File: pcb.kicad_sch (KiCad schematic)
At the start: 9 parts, among them SW1 SW_SPST

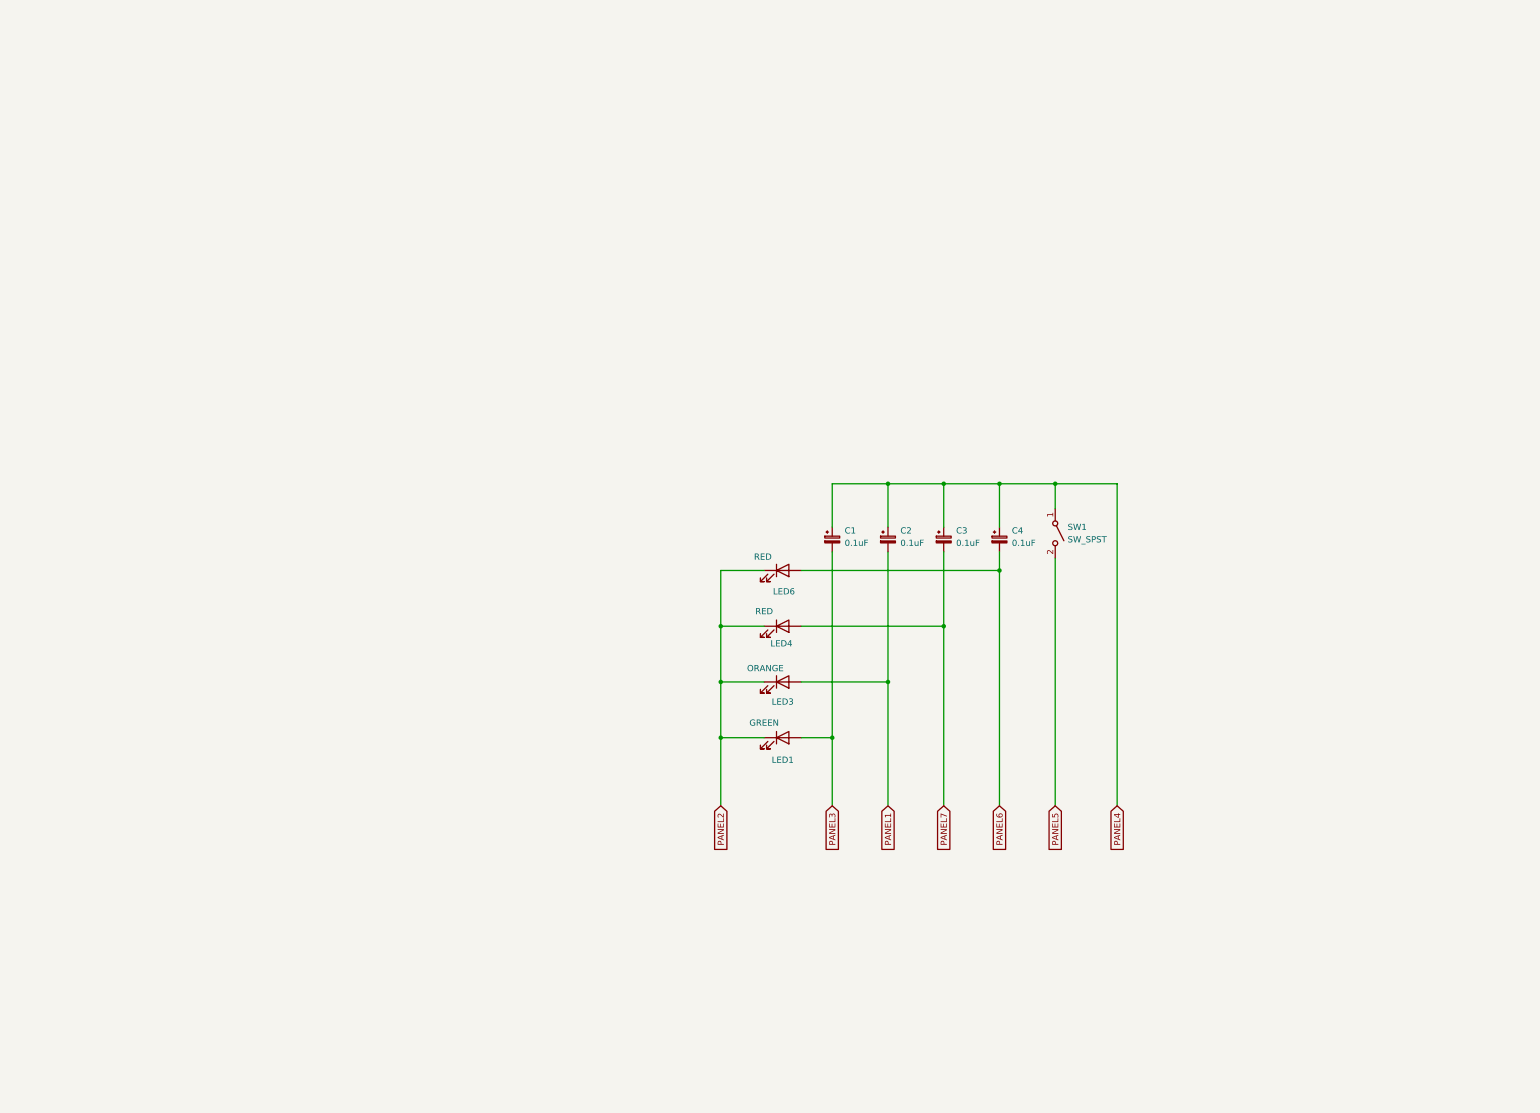
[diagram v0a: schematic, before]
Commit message: Move front panel to its own schematic page
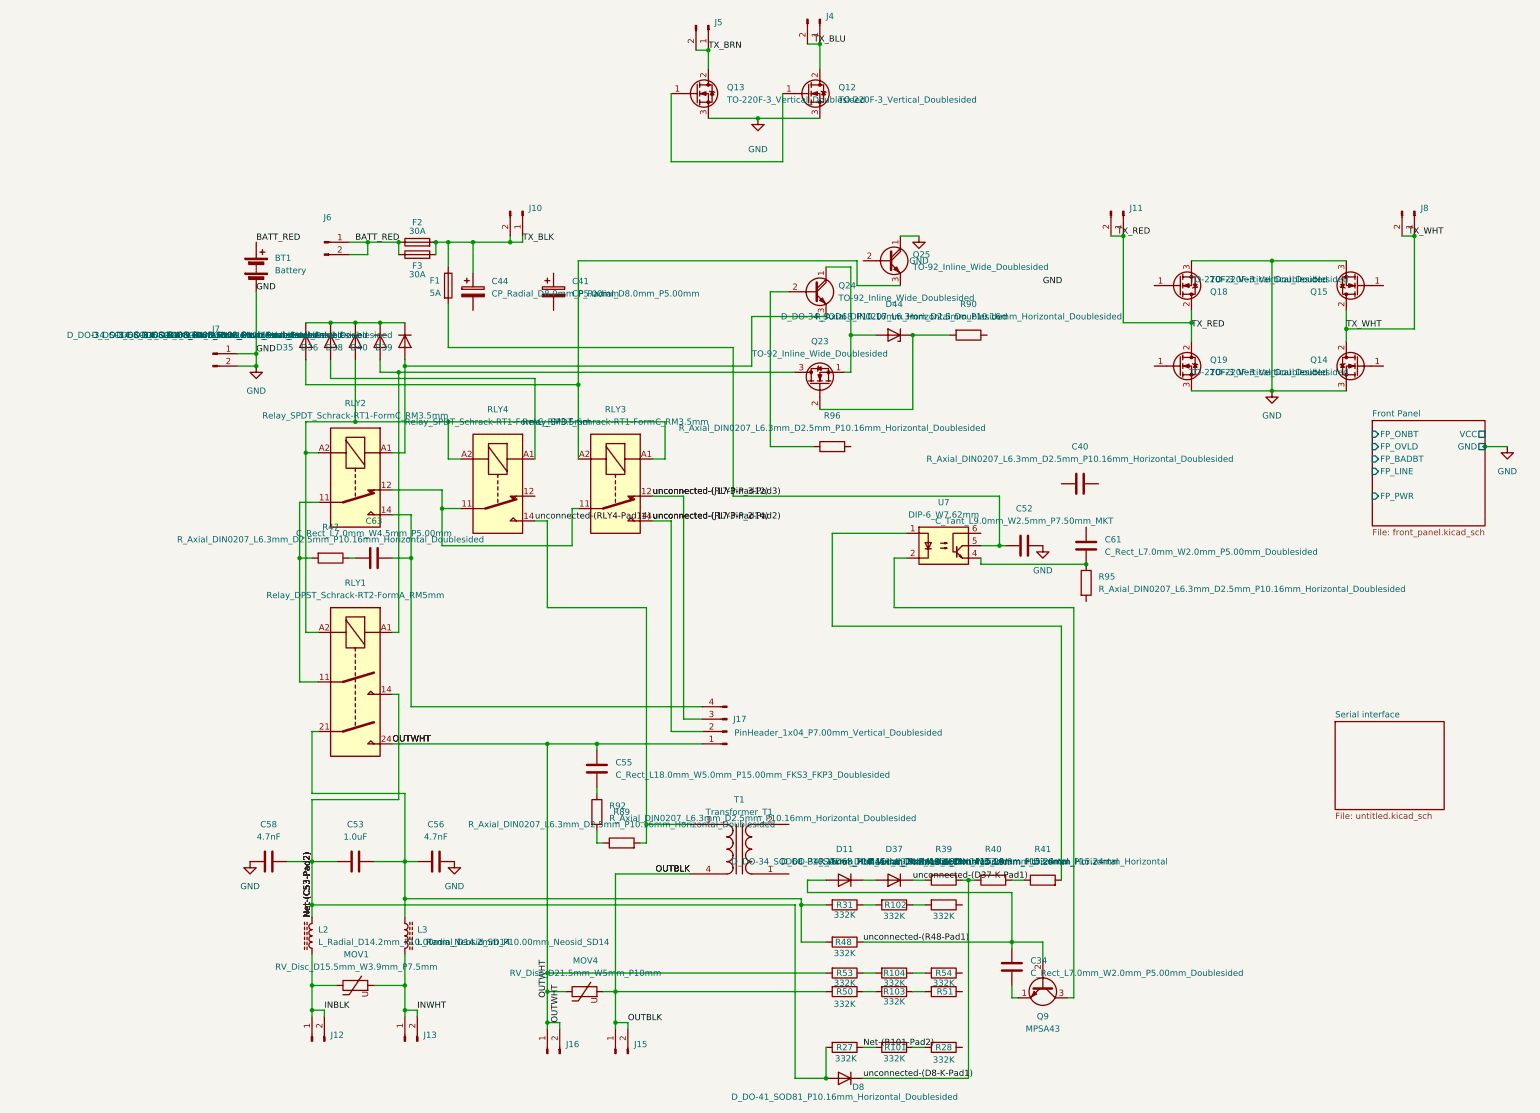
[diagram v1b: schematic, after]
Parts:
- removed C1, C2, C3, C4: 0.1uF, symbol Device:C_Polarized_Small
- removed LED1: GREEN, symbol Device:LED
- removed LED3: ORANGE, symbol Device:LED
- removed LED4, LED6: RED, symbol Device:LED
- removed SW1: SW_SPST, symbol Switch:SW_SPST
- added BT1: Battery, symbol Device:Battery
- added C34, C61: C_Rect_L7.0mm_W2.0mm_P5.00mm_Doublesided, apc-custom:C_Rect_L7.0mm_W2.0mm_P5.00mm_Doublesided, symbol Device:C
- added C40: R_Axial_DIN0207_L6.3mm_D2.5mm_P10.16mm_Horizontal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, apc-custom:C_Rect_L7.2mm_W3.0mm_P5.00mm_FKS2_FKP2_MKS2_MKP2_Doublesided, symbol Device:C
- added C41, C44: CP_Radial_D8.0mm_P5.00mm, Capacitor_THT:CP_Radial_D8.0mm_P5.00mm, symbol Device:C_Polarized
- added C52: C_Tant_L9.0mm_W2.5mm_P7.50mm_MKT, apc-custom:C_Tant_L9.0mm_W2.5mm_P7.50mm_MKT, symbol Device:C
- added C53: 1.0uF, apc-custom:C_Rect_L31.5mm_W13.0mm_P27.50mm_MKS4_Doublesided, symbol Device:C
- added C55: C_Rect_L18.0mm_W5.0mm_P15.00mm_FKS3_FKP3_Doublesi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, apc-custom:C_Rect_L18.0mm_W5.0mm_P15.00mm_FKS3_FKP3_Doublesided, symbol Device:C
- added C56, C58: 4.7nF, Capacitor_THT:C_Disc_D10.0mm_W2.5mm_P5.00mm, symbol Device:C
- added C63: C_Rect_L7.0mm_W4.5mm_P5.00mm, Capacitor_THT:C_Rect_L7.0mm_W4.5mm_P5.00mm, symbol Device:C
- added D11, D35, D36, D37, D38, D39, D40: D_DO-34_SOD68_P10.16mm_Horizontal_Doublesided, apc-custom:D_DO-34_SOD68_P10.16mm_Horizontal_Doublesided, symbol Device:D
- added D44: D_DO-34_SOD68_P10.16mm_Horizontal_Doublesided, apc-custom:D_DO-34_SOD68_P10.16mm_Horizontal_Doublesided, symbol Device:D_Zener
- added D8: D_DO-41_SOD81_P10.16mm_Horizontal_Doublesided, apc-custom:D_DO-41_SOD81_P10.16mm_Horizontal_Doublesided, symbol Device:D
- added F1: 5A, apc-custom:Fuse_PCB_P8.00mm, symbol Device:Fuse
- added F2, F3: 30A, Fuse:Fuse_Blade_ATO_directSolder, symbol Device:Fuse
- added J10, J11, J12, J13, J15, J16, J4, J5, J6, J7, J8: ~, apc-custom:keystone-FASTON, symbol Connector:Conn_01x02_Pin
- added J17: PinHeader_1x04_P7.00mm_Vertical_Doublesided, apc-custom:PinHeader_1x04_P7.00mm_Vertical_Doublesided, symbol Connector:Conn_01x04_Pin
- added L2, L3: L_Radial_D14.2mm_P10.00mm_Neosid_SD14, Inductor_THT:L_Radial_D14.2mm_P10.00mm_Neosid_SD14, symbol Device:L_Ferrite
- added MOV1: RV_Disc_D15.5mm_W3.9mm_P7.5mm, Varistor:RV_Disc_D15.5mm_W3.9mm_P7.5mm, symbol Device:Varistor
- added MOV4: RV_Disc_D21.5mm_W5mm_P10mm, Varistor:RV_Disc_D21.5mm_W5mm_P10mm, symbol Device:Varistor
- added Q12, Q13: TO-220F-3_Vertical_Doublesided, apc-custom:TO-220F-3_Vertical_Doublesided, symbol apc-custom:IRFZ34N
- added Q14, Q15, Q18, Q19: TO-220F-3_Vertical_Doublesided, Package_TO_SOT_THT:TO-220-3_Vertical, symbol apc-custom:PHP54N06T
- added Q23: TO-92_Inline_Wide_Doublesided, apc-custom:TO-92_Inline_Wide_Doublesided, symbol Transistor_FET:2N7000
- added Q24, Q25: TO-92_Inline_Wide_Doublesided, apc-custom:TO-92_Inline_Wide_Doublesided, symbol Transistor_BJT:BC517
- added Q9: MPSA43, Package_TO_SOT_THT:TO-92_Inline, symbol apc-custom:MPSA43
- added R101, R102, R103, R104, R27, R28, R31, R32, R48, R50, R53, R54: 332K, apc-custom:R_Axial_DIN0207_L6.3mm_D2.5mm_P10.16mm_Horizontal_Doublesided, symbol Device:R
- added R39, R40, R41: R_Axial_DIN0411_L9.9mm_D3.6mm_P15.24mm_Horizontal, Resistor_THT:R_Axial_DIN0411_L9.9mm_D3.6mm_P15.24mm_Horizontal, symbol Device:R
- added R47, R51, R89, R90, R92, R95, R96: R_Axial_DIN0207_L6.3mm_D2.5mm_P10.16mm_Horizontal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, apc-custom:R_Axial_DIN0207_L6.3mm_D2.5mm_P10.16mm_Horizontal_Doublesided, symbol Device:R
- added RLY1: Relay_DPST_Schrack-RT2-FormA_RM5mm, Relay_THT:Relay_DPST_Schrack-RT2-FormA_RM5mm, symbol Relay:RT44xxxx
- added RLY2, RLY3, RLY4: Relay_SPDT_Schrack-RT1-FormC_RM3.5mm, Relay_THT:Relay_SPDT_Schrack-RT1-FormC_RM3.5mm, symbol Relay:RT314A12
- added T1: Transformer_T1, apc-custom:Transformer_T1, symbol Device:Transformer_1P_1S
- added U7: DIP-6_W7.62mm, Package_DIP:DIP-6_W7.62mm, symbol Isolator:4N25
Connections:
- new net: C53.1, C56.1, L3.1, R31.2, R48.2, RLY1.21
- new net: R103.1, R51.2
- new net: R103.2, R50.1
- new net: D44.2 (A), Q23.1 (S), Q24.1 (C)
- new net: Q24.2 (B), R96.1
- new net: D39.2 (A), Q24.3 (E), RLY2.A1
- new net: D44.1 (K), Q23.2 (G), R90.2
- new net: R102.2, R31.1
- new net: R40.1, R41.1
- new net: C52.2, F1.2, U7.5
- new net: Q12.1 (G), Q13.1 (G)
- new net: D35.1 (K), D36.1 (K), D38.1 (K), D39.1 (K), D40.1 (K)
- new net: RLY2.12, RLY3.11, RLY4.11
- new net: D38.2 (A), RLY1.A2, RLY2.A2, RLY3.A1, RLY4.A2
- new net: D35.2 (A), Q25.3 (E), RLY3.A2
- new net: D40.2 (A), Q23.3 (D), RLY1.A1
- new net: C34.1, Q9.1 (E)
- new net: C63.1, J17.4 (Pin_4), RLY2.14
- new net: C63.2, R47.1
- new net: Q9.3 (C), U7.2
- new net: R47.2, RLY1.11, RLY2.11
- new net: R104.1, R54.2
- new net: R104.2, R53.1
- new net: D36.2 (A), RLY4.A1
- new net: C61.2, R95.1, U7.4
- new net: R89.1, R92.2
- new net: D11.1 (K), D37.2 (A)
- new net: C55.2, R92.1
- new net: R102.1, R32.2
- new net: R101.1, R28.2
- new net: R41.2, U7.1
- new net BATT_RED: BT1.1 (+), F2.1, F3.1, J6.1 (Pin_1), J6.2 (Pin_2)
- new net GND: BT1.2 (-), C52.1, C56.2, C58.1, J7.1 (Pin_1), J7.2 (Pin_2), Q12.3 (S), Q13.3 (S), Q14.3 (S), Q15.3 (S), Q18.3 (S), Q19.3 (S), Q25.1 (C)
- new net INBLK: J12.1 (Pin_1), J12.2 (Pin_2), L2.1, MOV1.1
- new net INWHT: J13.1 (Pin_1), J13.2 (Pin_2), L3.2, MOV1.2
- new net Net-(C53-Pad2): C53.2, C58.2, D8.2 (A), L2.2, R27.2, RLY1.14
- new net Net-(R101-Pad2): R101.2, R27.1
- new net OUTBLK: J15.1 (Pin_1), J15.2 (Pin_2), MOV4.2, R50.2, T1.4 (SB)
- new net OUTWHT: C55.1, J16.1 (Pin_1), J16.2 (Pin_2), J17.1 (Pin_1), MOV4.1, R53.2, RLY1.24
- new net TX_BLK: C44.1, F1.1, F2.2, F3.2, J10.1 (Pin_1), J10.2 (Pin_2)
- new net TX_BLU: J4.1 (Pin_1), J4.2 (Pin_2), Q12.2 (D)
- new net TX_BRN: J5.1 (Pin_1), J5.2 (Pin_2), Q13.2 (D)
- new net TX_RED: J11.1 (Pin_1), J11.2 (Pin_2), Q18.2 (D), Q19.2 (D)
- new net TX_WHT: J8.1 (Pin_1), J8.2 (Pin_2), Q14.2 (D), Q15.2 (D)
- new net unconnected-(D37-K-Pad1): D37.1 (K), R39.2
- new net unconnected-(D8-K-Pad1): D8.1 (K), R39.1, R40.2
- new net unconnected-(J17-Pin_2-Pad2): J17.2 (Pin_2), RLY3.14
- new net unconnected-(J17-Pin_3-Pad3): J17.3 (Pin_3), RLY3.12
- new net unconnected-(R48-Pad1): C34.2, D11.2 (A), Q9.2 (B), R48.1
- new net unconnected-(RLY4-Pad14): R89.2, RLY4.14, T1.3 (SA)
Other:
- added sheet Front Panel (front_panel.kicad_sch)
- added sheet Serial interface (untitled.kicad_sch)

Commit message: Almost all components added to schematic. Some traces and an IC missing.
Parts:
- removed C53: 1.0uF, apc-custom:C_Rect_L31.5mm_W13.0mm_P27.50mm_MKS4_Doublesided, symbol Device:C
- removed C56, C58: 4.7nF, Capacitor_THT:C_Disc_D10.0mm_W2.5mm_P5.00mm, symbol Device:C
- removed L2, L3: L_Radial_D14.2mm_P10.00mm_Neosid_SD14, Inductor_THT:L_Radial_D14.2mm_P10.00mm_Neosid_SD14, symbol Device:L_Ferrite
- removed MOV1: RV_Disc_D15.5mm_W3.9mm_P7.5mm, Varistor:RV_Disc_D15.5mm_W3.9mm_P7.5mm, symbol Device:Varistor
- removed RLY1: Relay_DPST_Schrack-RT2-FormA_RM5mm, Relay_THT:Relay_DPST_Schrack-RT2-FormA_RM5mm, symbol Relay:RT44xxxx
- added BP1: MagneticBuzzer_ProSignal_ABT-410-RC, Buzzer_Beeper:MagneticBuzzer_ProSignal_ABT-410-RC, symbol Device:Buzzer
- added C10, C11, C12, C21, C22, C23, C57, C60, C62, C67, C9: C_Tant_L9.0mm_W2.5mm_P7.50mm_MKT, apc-custom:C_Tant_L9.0mm_W2.5mm_P7.50mm_MKT, symbol Device:C
- added C13, C14, C32: C_Disc_D4.7mm_W2.5mm_P5.00mm_Doublesided, apc-custom:C_Disc_D4.7mm_W2.5mm_P5.00mm_Doublesided, symbol Device:C
- added C15, C42: C_Radial_D12.5mm_H25.0mm_P5.00mm_Doublesided, apc-custom:C_Radial_D12.5mm_H25.0mm_P5.00mm_Doublesided, symbol Device:C_Polarized
- added C24, C68: C_Tant_L5.0mm_W2.5mm_P5.0mm_MKT_Doublesided, apc-custom:C_Tant_L5.0mm_W2.5mm_P5.0mm_MKT_Doublesided, symbol Device:C
- added C25, C27, C28, C29, C33, C36, C37, C39, C43, C45, C47, C48, C51: C_Rect_L7.0mm_W2.0mm_P5.00mm_Doublesided, apc-custom:C_Rect_L7.0mm_W2.0mm_P5.00mm_Doublesided, symbol Device:C
- added C30, C31, C35, C38, C49, C50: C_Radial_D4.0mm_H7.0mm_P5.00mm_Doublesided, apc-custom:C_Radial_D4.0mm_H7.0mm_P5.00mm_Doublesided, symbol Device:C_Polarized
- added C46: C, symbol Device:C
- added C5, C7, C8: 100nF, apc-custom:C_Tant_L9.0mm_W2.5mm_P7.50mm_MKT, symbol Device:C
- added C6: 100nF, apc-custom:C_Rect_L7.0mm_W2.0mm_P5.00mm_Doublesided, symbol Device:C
- added D10, D12, D13, D14, D15, D16, D25, D26, D27, D28, D29, D30, D31, D32, D33, D42, D45, D46, D7, D9: D_DO-34_SOD68_P10.16mm_Horizontal_Doublesided, apc-custom:D_DO-34_SOD68_P10.16mm_Horizontal_Doublesided, symbol Device:D
- added D17, D18, D19, D20, D21, D22, D23, D24: D_DO-41_SOD81_P10.16mm_Horizontal_Doublesided, apc-custom:D_DO-41_SOD81_P10.16mm_Horizontal_Doublesided, symbol Device:D
- added L1: Inductor_L1, apc-custom:Inductor_L1, symbol Device:L_Ferrite_Coupled
- added L4: L_Axial_L5.0mm_D3.6mm_P10.00mm_Horizontal_Murata_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, Inductor_THT:L_Axial_L5.0mm_D3.6mm_P10.00mm_Horizontal_Murata_BL01RN1A2A2, symbol Device:L
- added L5: L_Axial_L5.3mm_D2.2mm_P10.16mm_Horizontal_Vishay_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, apc-custom:L_Axial_L5.3mm_D2.2mm_P10.16mm_Horizontal_Vishay_IM-1_Doublesided, symbol Device:L
- added Q1: TO-92_Inline_Wide_Doublesided, apc-custom:TO-92_Inline_Wide_Doublesided, symbol apc-custom:MPSA13
- added Q10, Q27, Q3, Q5, Q7: TO-92_Inline_Wide_Doublesided, apc-custom:TO-92_Inline_Wide_Doublesided, symbol apc-custom:KSP2222A
- added Q11, Q2, Q26, Q4, Q6: TO-92_Inline_Wide_Doublesided, apc-custom:TO-92_Inline_Wide_Doublesided, symbol apc-custom:KSP2907A
- added Q28, Q8: TO-92_Inline_Wide_Doublesided, apc-custom:TO-92_Inline_Wide_Doublesided, symbol Transistor_FET:2N7000
- added R1, R100, R105, R106, R107, R108, R12, R13, R16, R17, R18, R19, R2, R20, R21, R22, R23, R24, R26, R29, R3, R30, R33, R34, R36, R37, R38, R4, R42, R43, R44, R45, R46, R49, R5, R52, R55, R56, R57, R58, R59, R6, R60, R61, R62, R63, R64, R66, R67, R68, R69, R7, R70, R71, R72, R73, R74, R75, R76, R77, R78, R79, R8, R82, R83, R86, R87, R88, R9, R91, R97, R98, R99: R_Axial_DIN0207_L6.3mm_D2.5mm_P10.16mm_Horizontal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, apc-custom:R_Axial_DIN0207_L6.3mm_D2.5mm_P10.16mm_Horizontal_Doublesided, symbol Device:R
- added R65: R_Axial_DIN0516_L15.5mm_D5.0mm_P20.32mm_Horizonta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, apc-custom:R_Axial_DIN0516_L15.5mm_D5.0mm_P20.32mm_Horizontal_Doublesided, symbol Device:R
- added U1: DIP-40_W15.24mm_Socket, Package_DIP:DIP-40_W15.24mm_Socket, symbol apc-custom:P87C51FB-4N_SOCKETED
- added U2: DIP-24_W7.62mm, Package_DIP:DIP-24_W7.62mm, symbol apc-custom:ADC0848CCN
- added U3: DIP-8_W7.62mm, Package_DIP:DIP-8_W7.62mm, symbol Memory_EEPROM:93CxxA
- added U5: TO-92_Inline_Wide_Doublesided, apc-custom:TO-92_Inline_Wide_Doublesided, symbol Power_Supervisor:MC34064P
- added U6: DIP-14_W7.62mm_Doublesided, apc-custom:DIP-14_W7.62mm_Doublesided, symbol apc-custom:LM324AN
- added U8: TO-220F-5_P3.4x3.7mm_StaggerEven_Lead3.5mm_Vertic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, Package_TO_SOT_THT:TO-220F-5_P3.4x3.7mm_StaggerEven_Lead3.5mm_Vertical, symbol apc-custom:LM2575T-ADJ
- added U9: DIP-14_W7.62mm_Doublesided, apc-custom:DIP-14_W7.62mm_Doublesided, symbol apc-custom:360-2040B
- added VR1: TO-92_Inline_Wide_Doublesided, apc-custom:TO-92_Inline_Wide_Doublesided, symbol Regulator_Linear:LP2950-5.0_TO92
- added Y1: Crystal_HC52-U_Vertical, Crystal:Crystal_HC52-U_Vertical, symbol Device:Crystal
- C41, C44: value CP_Radial_D8.0mm_P5.00mm -> 330uF 25V
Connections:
- net Front Panel/FP_BADBT: now also R7.1
- net Front Panel/FP_LINE: now also R4.1
- net Front Panel/FP_ONBT: now also R5.1
- net Front Panel/FP_OVLD: now also R6.1
- net Front Panel/FP_PWR: now also R17.1
- net Front Panel/VCC: now also C7.2, R2.2
- net GND: now also C40.1, C41.2, C44.2, C10.2, C11.2, C12.2, C15.2, C21.1, C22.1, C25.1, C28.2, C29.2, C30.2, C31.2, C33.2, C35.2, C37.2, C42.2, C43.2, C45.2, C46.1, C47.1, C48.2, C50.1, C51.1, C57.2, C6.1, C60.1, C62.2, C67.2, C68.1, C7.1, C9.2, D13.2 (A), D19.2 (A), D20.2 (A), D29.1 (K), D32.2 (A), D33.2 (A), D45.2 (A), Q1.1 (C), Q27.1 (E), Q5.1 (E), Q7.1 (E), Q8.1 (S), R100.2, R24.2, R33.1, R44.1, R45.1, R49.1, R57.1, R62.1, R67.1, R69.2, R74.2, R77.2, R8.2, R88.1, U2.10 (AGND), U2.12 (DGND), U3.5 (GND), U5.3 (GND), U6.12 (+), U6.5 (+), U8.3 (GND), U9.5, VR1.2 (GND)
- net TX_BLK: now also D17.1 (K), D18.1 (K)
- net TX_BLU: now also D16.1 (K), D21.2 (A), D22.2 (A)
- net TX_BRN: now also D23.2 (A), D24.2 (A)
- net TX_RED: now also D25.1 (K)
- net TX_WHT: now also D27.1 (K)
- net at C41.1: now also D17.2 (A), D18.2 (A), L1.2, L1.4, R66.1
- net Line in/LIVE_SENSE: now reaches R31.2, R48.2
- net at Q18.1 (G): now also R82.1
- net Line in/RLY_LINE_2: now reaches C52.2, F1.2, U7.5
- net Line in/RLY_LINE_2: now also RLY2.A2, RLY3.A1, RLY4.A2, Q2.1 (C), Q6.1 (C), R36.2
- net at R51.1: now also C36.1, R52.2, U6.9 (-)
- net at Q19.1 (G): now also R83.1
- net Line in/RLY_LINE_1: now reaches D40.2 (A), Q23.3 (D)
- net at Q15.1 (G): now also R79.1
- net Line in/SW_NEUTRAL: now reaches R47.2, RLY2.11
- net at D36.2 (A), RLY4.A1: now also Q27.3 (C)
- net at C61.2, R95.1, U7.4: now also R43.1
- net at R95.2: now also C61.1, U7.6
- net at T1.1 (AA): now also D30.2 (A), D32.1 (K)
- net at T1.2 (AB): now also D31.2 (A), D33.1 (K)
- net at C40.2: now also R60.1, R61.1
- net at R54.1: now also C37.1, R57.2, U6.10 (+)
- net at Q25.2 (B): now also R97.1
- net at Q14.1 (G): now also R78.1
- net at R28.1: now also C27.2, R26.1, U6.2 (-)
- net at R32.1: now also C28.1, R33.2, U6.3 (+)
- net Net-(C53-Pad2) renamed Line in/NEUTRAL_SENSE
- net Net-(R101-Pad2): no longer names the net of R101.2, R27.1
- net unconnected-(D37-K-Pad1): no longer names the net of D37.1 (K), R39.2
- net unconnected-(D8-K-Pad1): no longer names the net of D8.1 (K), R39.1, R40.2
- net unconnected-(J17-Pin_2-Pad2): no longer names the net of J17.2 (Pin_2), RLY3.14
- net unconnected-(J17-Pin_3-Pad3): no longer names the net of J17.3 (Pin_3), RLY3.12
- net unconnected-(R48-Pad1): no longer names the net of C34.2, D11.2 (A), Q9.2 (B), R48.1
- net unconnected-(RLY4-Pad14): no longer names the net of R89.2, RLY4.14, T1.3 (SA)
- new net: C33.1, D12.1 (K), Q8.2 (G), R45.2
- new net: C31.1, R38.1, VR1.3 (VI)
- new net: R29.1, R30.1, U6.6 (-)
- new net: D10.1 (K), D7.2 (A), R30.2, U2.3 (CH2)
- new net: Q10.1 (E), R59.2, R62.2
- new net: R70.2, U9.8
- new net: R73.1, R82.2, R83.2, U9.12
- new net: Q4.2 (B), R21.1, R23.1
- new net: C25.2, R23.2, U5.1 (~{RESET})
- new net: Q7.2 (B), Q8.3 (D), R38.2, R42.2, R43.2, R44.2
- new net: R72.1, R78.2, R79.2, U9.10
- new net: C35.1, C60.2, R46.2, R49.2, U2.2 (CH1)
- new net: C46.2, U9.2
- new net: D45.1 (K), Q28.2 (G), U1.4 (P1.3/CEX0)
- new net: C15.1, C39.1, C42.1, C43.1, D21.1 (K), D22.1 (K), D23.1 (K), D24.1 (K), Q11.1 (C), R3.1, R65.1
- new net: C29.1, C30.1, C38.1, D14.1 (K), D7.1 (K), Q26.1 (C), R34.2, R58.2, R76.2, VR1.1 (VO)
- new net: Q28.3 (D), R86.2, R87.2
- new net: D19.1 (K), D20.1 (K), L1.1, L1.3, U8.2 (OUT)
- new net: Q4.1 (C), R22.1
- new net: C24.1, Q4.3 (E), R24.1, U1.9 (RST)
- new net: D16.2 (A), Q10.2 (B), R63.2
- new net: C49.1, R1.1, R75.1, U9.14 (VCC)
- new net: C48.1, R75.2, U9.13
- new net: C10.1, R6.2, U1.37 (P0.2/AD2)
- new net: C36.2, R52.1, R55.2, U6.8
- new net: C45.1, D26.1 (K), D46.1 (K), R69.1, U9.7 (GND)
- new net: Q6.2 (B), R36.1, R37.1
- new net: C22.2, C57.1, Q6.3 (E), R46.1, U6.4 (V+), U9.1
- new net: C23.1, R12.1, R13.1, R18.1, R9.1
- new net: Q2.3 (E), R19.1, R42.1
- new net: Q11.2 (B), R64.1
- new net: C39.2, Q11.3 (E), R60.2
- new net: BP1.1 (+), C8.1, D42.2 (A), R16.1
- new net: C8.2, Q2.2 (B), R16.2, R17.2
- new net: C38.2, Q10.3 (C), R58.1, U2.4 (CH3)
- new net: C12.1, R4.2, U1.39 (P0.0/AD0)
- new net: Q1.2 (B), R108.1
- new net: R1.2, R108.2
- new net: R55.1, R56.1, U6.13 (-)
- new net: C6.2, R3.2, R8.1
- new net: Q3.3 (C), R18.2
- new net: D25.2 (A), D26.2 (A), R73.2
- new net: R63.1, R68.1
- new net: C51.2, R87.1, U2.7 (CH8)
- new net: R64.2, R65.2, U8.1 (VIN)
- new net: D27.2 (A), D46.2 (A), R72.2
- new net: Q26.2 (B), R98.2
- new net: Q26.3 (E), R99.2
- new net: C13.1, C14.1
- new net: C14.2, U1.18 (XTAL2), Y1.1
- new net: C62.1, C68.2, L4.1, U2.24 (VCC)
- new net: D30.1 (K), D31.1 (K), R88.2
- new net: R61.2, R66.2, R67.2, U8.4 (FB)
- new net: C32.2, D12.2 (A), D13.1 (K)
- new net: BP1.2 (-), D42.1 (K), Q1.3 (E)
- new net: R71.2, U9.9
- new net: C27.1, D9.1 (K), R26.2, R29.2, U6.1
- new net: D9.2 (A), Q5.2 (B), R34.1
- new net: D14.2 (A), D15.1 (K), R56.2
- new net: D15.2 (A), U6.14
- new net: R91.2, U1.11 (P3.1/TXD)
- new net: C47.2, U9.4
- new net: Q27.2 (B), R100.1, R99.1
- new net: R107.1, U8.5 (~{ON}/OFF)
- new net: R76.1, R77.1, U9.6
- new net: C13.2, U1.19 (XTAL1), Y1.2
- new net: C50.2, D28.2 (A), U6.11 (V-)
- new net: R105.1, U1.14 (P3.4/T0), U3.1 (CS)
- new net: U1.15 (P3.5/T1), U3.2 (SCLK)
- new net: R107.2, U1.16 (P3.6/~{WR}), U3.4 (DO)
- new net: C9.1, R7.2, U1.36 (P0.3/AD3)
- new net: D10.2 (A), U6.7
- new net: R98.1, U1.13 (P3.3/~{INT1})
- new net: C49.2, D28.1 (K), D29.2 (A)
- new net: Q7.3 (C), R37.2
- new net: R106.2, U1.10 (P3.0/RXD)
- new net: C32.1, R105.2
- new net: Q3.2 (B), R19.2, R20.1
- new net: C23.2, Q3.1 (E), R20.2
- new net: C11.1, R5.2, U1.38 (P0.1/AD1)
- new net VCC: C24.2, C5.2, C67.1, L4.2, L5.1, L5.2, R2.1, R21.2, R22.2, R59.1, R70.1, R71.1, R9.2, U1.31 (~{EA}/VPP), U1.40 (VCC), U3.8 (VCC), U5.2 (IN)
- now unconnected: D38.2 (A)
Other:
- added sheet Line in (line-in.kicad_sch)
- moved on the sheet: C34, C44, C52, C55, C61, D44, D8, J10, J15, J16, J4, J5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
